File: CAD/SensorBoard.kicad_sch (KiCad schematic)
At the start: 0 parts

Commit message: Add MCU symbol
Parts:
- added MCU1: STM32U073CCT6, Package_QFP:LQFP-48_7x7mm_P0.5mm, symbol SensorBoard:STM32U073CCT6
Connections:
- new net: MCU1.23 (VSS), MCU1.35 (VSS), MCU1.47 (VSS)
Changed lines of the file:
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@@
 		(company "Cristian Cristea")
+	)
+	(symbol
+		(lib_id "SensorBoard:STM32U073CCT6")
+		(at 209.55 134.62 0)
+		(unit 1)
+		(exclude_from_sim no)
+		(in_bom yes)
+		(on_board yes)
+		(dnp no)
+		(property "Reference" "MCU1"
+			(at 195.58 92.964 0)
+			(effects
+				(font
+					(size 1.27 1.27)
+				)
+				(justify left)
+			)
+		)
+		(property "Value" " STM32U073CCT6 "
+			(at 204.47 147.32 0)
+			(effects
+				(font
+					(size 1.27 1.27)
+				)
+				(justify left)
+			)
+		)
+		(property "Footprint" "Package_QFP:LQFP-48_7x7mm_P0.5mm"
+			(at 196.85 170.18 0)
+			(effects
+				(font
+					(size 1.27 1.27)
+				)
+				(justify right)
+				(hide yes)
+			)
+		)
+		(property "Datasheet" "https://www.st.com/resource/en/datasheet/stm32u073cc.pdf"
+			(at 209.55 134.62 0)
+			(effects
+				(font
+					(size 1.27 1.27)
+				)
+				(hide yes)
+			)
+		)
+		(property "Description" "STMicroelectronics Arm Cortex-M0+ MCU, 256KB flash, 40KB RAM, 56 MHz, 1.71-3.6V, 37 GPIO, LQFP48"
+			(at 209.55 134.62 0)
+			(effects
+				(font
+					(size 1.27 1.27)
+				)
+				(hide yes)
+			)
+		)
+		(pin "33"
+		)
+		(pin "25"
+		)
+		(pin "46"
+		)
+		(pin "6"
+		)
+		(pin "14"
+		)
+		(pin "37"
+		)
+		(pin "48"
+		)
+		(pin "2"
+		)
+		(pin "42"
+		)
+		(pin "45"
+		)
+		(pin "5"
+		)
+		(pin "47"
+		)
+		(pin "21"
+		)
+		(pin "12"
+		)
+		(pin "43"
+		)
+		(pin "44"
+		)
+		(pin "10"
+		)
+		(pin "1"
+		)
+		(pin "13"
+		)
+		(pin "15"
+		)
+		(pin "11"
+		)
+		(pin "4"
+		)
+		(pin "31"
+		)
+		(pin "20"
+		)
+		(pin "16"
+		)
+		(pin "7"
+		)
+		(pin "41"
+		)
+		(pin "19"
+		)
+		(pin "39"
+		)
+		(pin "18"
+		)
+		(pin "3"
+		)
+		(pin "28"
+		)
+		(pin "17"
+		)
+		(pin "30"
+		)
+		(pin "22"
+		)
+		(pin "8"
+		)
+		(pin "34"
+		)
+		(pin "23"
+		)
+		(pin "24"
+		)
+		(pin "36"
+		)
+		(pin "9"
+		)
+		(pin "26"
+		)
+		(pin "27"
+		)
+		(pin "29"
+		)
+		(pin "40"
+		)
+		(pin "32"
+		)
+		(pin "35"
+		)
+		(pin "38"
+		)
+		(instances
+			(project ""
+				(path "/56f2708f-e6aa-4b97-8a34-e15d8ff6695d"
+					(reference "MCU1")
+					(unit 1)
+				)
+			)
+		)
 	)
 	(sheet_instances

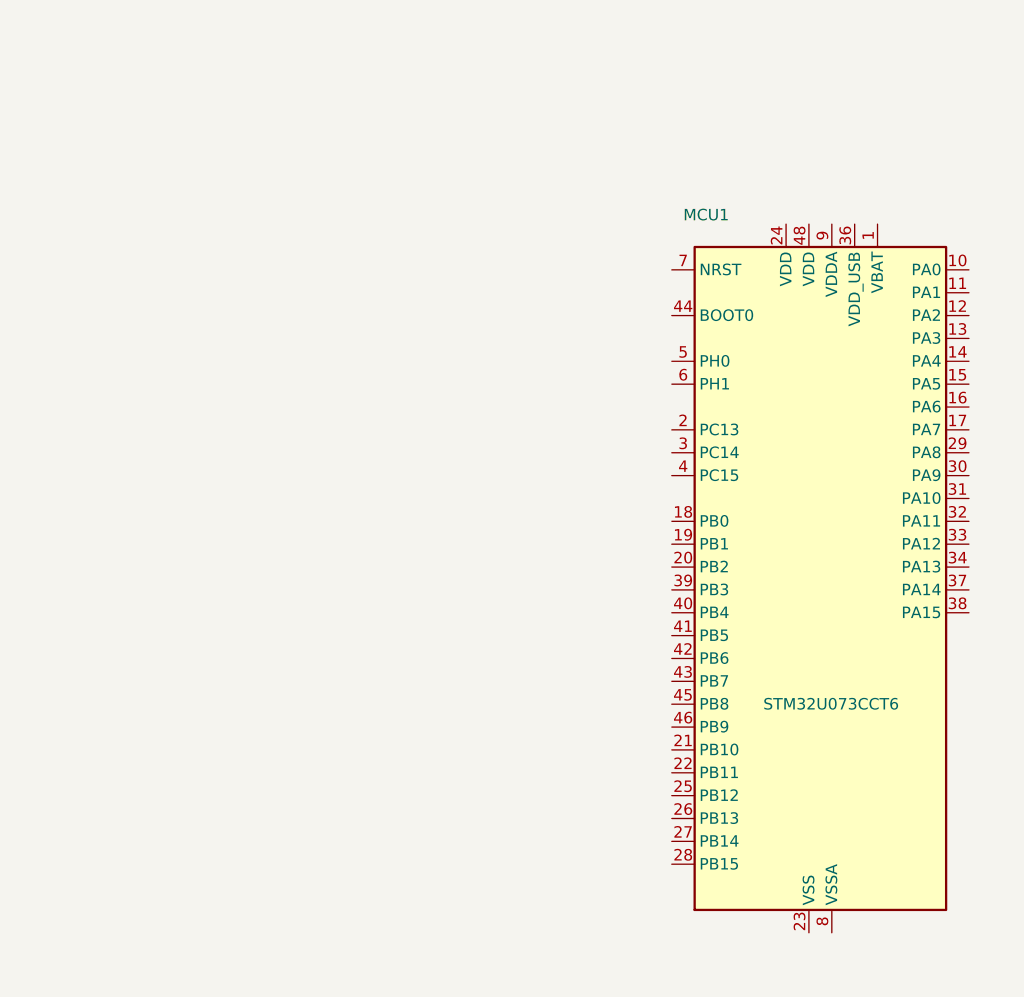
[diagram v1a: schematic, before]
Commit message: Add crystal oscillators to schematic
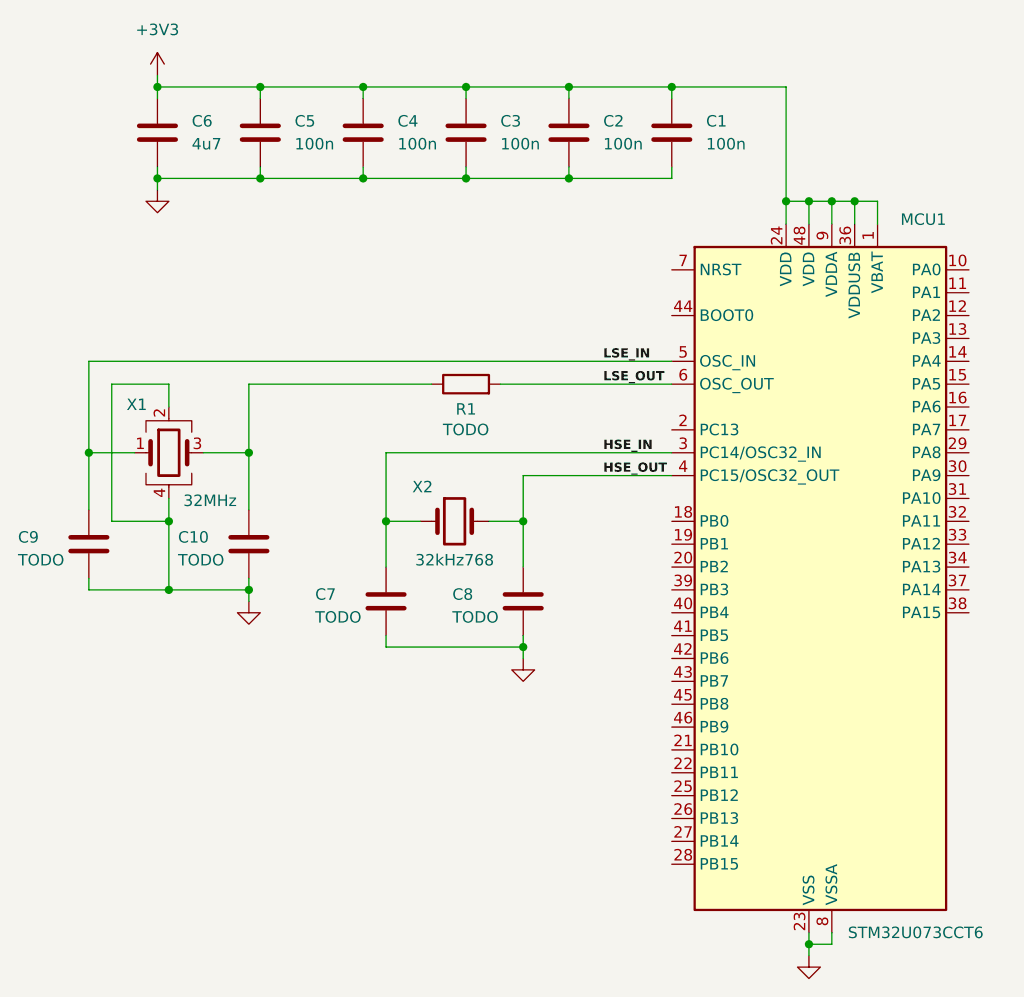
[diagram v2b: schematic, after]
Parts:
- added C1, C2, C3, C4, C5: 100n, symbol Device:C
- added C10, C7, C8, C9: TODO, symbol Device:C
- added C6: 4u7, symbol Device:C
- added R1: TODO, symbol Device:R
- added X1: 32MHz, symbol Device:Crystal_GND24
- added X2: 32kHz768, symbol Device:Crystal
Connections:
- net +3V3: now reaches MCU1.1 (VBAT)
- net +3V3: now also MCU1.24 (VDD), MCU1.36 (VDDUSB), MCU1.48 (VDD), MCU1.9 (VDDA), C1.1, C2.1, C3.1, C4.1, C5.1, C6.1
- net GND: now reaches MCU1.23 (VSS), MCU1.35 (VSS), MCU1.47 (VSS)
- net GND: now also MCU1.8 (VSSA), C1.2, C10.2, C2.2, C3.2, C4.2, C5.2, C6.2, C7.2, C8.2, C9.2, X1.2, X1.4
- net HSE_IN: now reaches MCU1.3 (PC14/OSC32_IN)
- net HSE_IN: now also C7.1, X2.1
- net HSE_OUT: now reaches MCU1.4 (PC15/OSC32_OUT)
- net HSE_OUT: now also C8.1, X2.2
- net LSE_IN: now reaches MCU1.5 (OSC_IN)
- net LSE_IN: now also C9.1, X1.1
- net LSE_OUT: now reaches MCU1.6 (OSC_OUT)
- net LSE_OUT: now also R1.2
- new net: C10.1, R1.1, X1.3

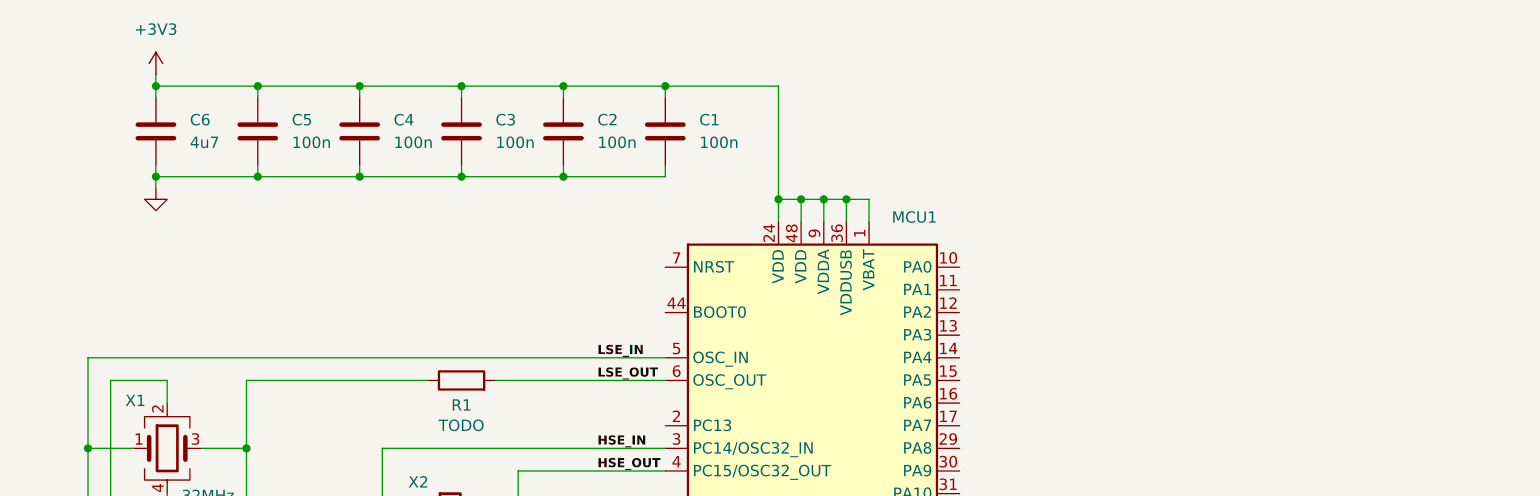
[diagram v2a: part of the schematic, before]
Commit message: Add BOOT button
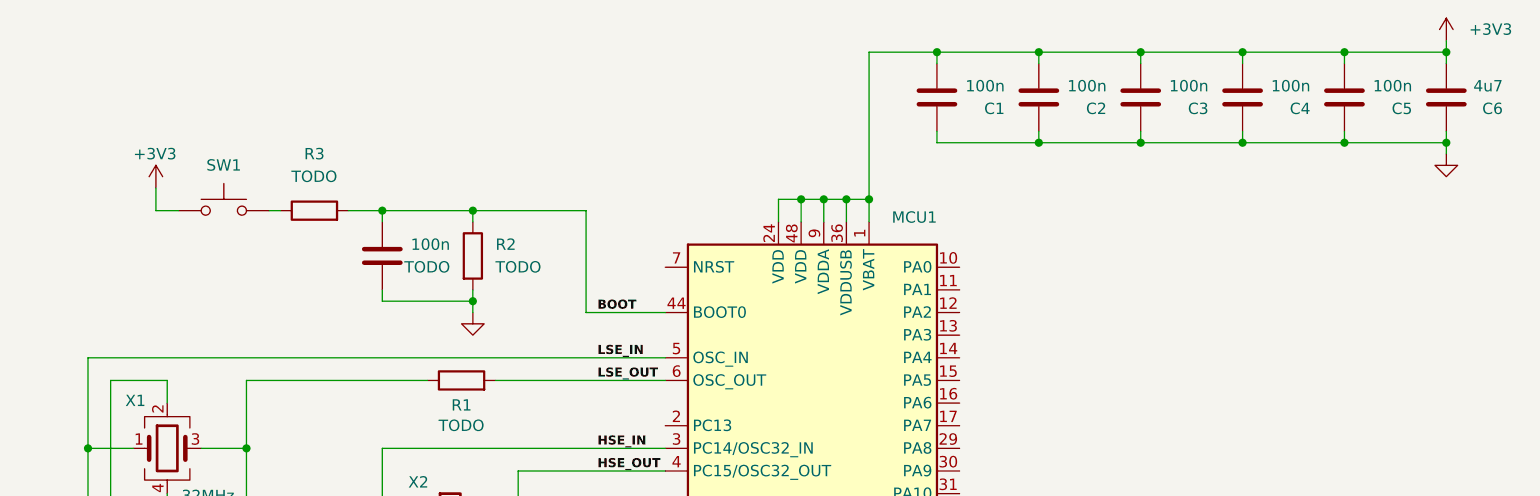
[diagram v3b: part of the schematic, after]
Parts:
- added R2, R3: TODO, symbol Device:R
- added SW1: BOOT_SW, symbol Switch:SW_Push
- added TODO: 100n, symbol Device:C
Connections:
- net +3V3: now also C1.2, C2.2, C3.2, C4.2, C5.2, C6.2, SW1.1; no longer C1.1, C2.1, C3.1, C4.1, C5.1, C6.1
- net GND: now also C1.1, C2.1, C3.1, C4.1, C5.1, C6.1, R2.2, TODO.1; no longer C1.2, C2.2, C3.2, C4.2, C5.2, C6.2
- net BOOT: now reaches MCU1.44 (BOOT0)
- net BOOT: now also R2.1, R3.2, TODO.2
- new net: R3.1, SW1.2
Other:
- moved on the sheet: C1, C2, C3, C4, C5, C6

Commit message: Further progress with power and peripherals
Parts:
- added C12, C13: 1u, symbol Device:C
- added C14: 100n, symbol Device:C
- added D1, D2: LED, symbol Device:LED
- added D3: Inolux_IN-P55TATRGB, LED_SMD:LED_Inolux_IN-P55TATRGB_PLCC6_5.0x5.5mm_P1.8mm, symbol LED:Inolux_IN-P55TATRGB
- added J1: USB C 2.0, symbol SensorBoard:USB_C_Receptacle_USB2.0
- added R10, R8, R9: 200, symbol Device:R
- added R4, R5: 5k1, symbol Device:R
- added R6, R7: 1k, symbol Device:R
- added U1: USBLC6-2SC6, Package_TO_SOT_SMD:SOT-23-6, symbol Power_Protection:USBLC6-2SC6
- added U2: MIC5365-3.3YD5, Package_TO_SOT_SMD:SOT-23-5, symbol Regulator_Linear:MIC5365-3.3YD5
- added U3: BME680, Package_LGA:Bosch_LGA-8_3x3mm_P0.8mm_ClockwisePinNumbering, symbol Sensor:BME680
- added U4: TC1047xNB, Package_TO_SOT_SMD:SOT-23, symbol Sensor_Temperature:TC1047xNB
- R2: value TODO -> 5k1
- R3: value TODO -> 200
- renumbered TODO to C11
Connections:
- net +3V3: now also C13.2, C14.2, R6.1, U2.5 (VOUT), U4.1 (V_{DD})
- net BOOT: now also MCU1.7 (NRST); no longer MCU1.44 (BOOT0)
- net GND: now also C12.1, C13.1, C14.1, D1.1 (K), D2.1 (K), D3.1 (KB), D3.2 (KR), D3.3 (KG), J1.A1 (GND), J1.A12 (GND), J1.B1 (GND), J1.B12 (GND), J1.S1 (SHIELD), R4.2, R5.2, U1.2 (GND), U2.2 (GND), U4.3 (GND)
- net HSE_IN: now also C9.1, MCU1.5 (OSC_IN), X1.1; no longer C7.1, MCU1.3 (PC14/OSC32_IN), X2.1
- net HSE_OUT: now also MCU1.6 (OSC_OUT), R1.2; no longer C8.1, MCU1.4 (PC15/OSC32_OUT), X2.2
- net LSE_IN: now also C7.1, MCU1.3 (PC14/OSC32_IN), X2.1; no longer C9.1, MCU1.5 (OSC_IN), X1.1
- net LSE_OUT: now also C8.1, MCU1.4 (PC15/OSC32_OUT), X2.2; no longer MCU1.6 (OSC_OUT), R1.2
- net ADC_TMP: now reaches MCU1.12 (PA2)
- net ADC_TMP: now also U4.2 (V_{OUT})
- net I2C_SDA: now reaches MCU1.16 (PA6)
- net I2C_SCL: now reaches MCU1.17 (PA7)
- net UART_TX: now reaches MCU1.21 (PB10)
- net UART_RX: now reaches MCU1.22 (PB11)
- net LED_R: now reaches MCU1.29 (PA8)
- net LED_R: now also R10.1
- net LED_G: now reaches MCU1.30 (PA9)
- net LED_G: now also R8.1
- net LED_B: now reaches MCU1.31 (PA10)
- net LED_B: now also R9.1
- net USB_D-: now reaches MCU1.32 (PA11)
- net USB_D-: now also U1.6 (I/O1)
- net USB_D+: now reaches MCU1.33 (PA12)
- net USB_D+: now also U1.4 (I/O2)
- net SPI_SCK: now reaches MCU1.39 (PB3)
- net SPI_MISO: now reaches MCU1.40 (PB4)
- net SPI_MOSI: now reaches MCU1.41 (PB5)
- new net: D3.5 (AR), R10.2
- new net: D3.4 (AG), R8.2
- new net: D2.2 (A), R6.2
- new net: D3.6 (AB), R9.2
- new net: D1.2 (A), R7.2
- new net +5V: C12.2, J1.A4 (VBUS), J1.A9 (VBUS), J1.B4 (VBUS), J1.B9 (VBUS), R7.1, U1.5 (VBUS), U2.1 (VIN), U2.3 (EN)
- new net USB_CC1: J1.A5 (CC1), R5.1
- new net USB_CC2: J1.B5 (CC2), R4.1
- new net USB_CD+: J1.A6 (D+), J1.B6 (D+), U1.3 (I/O2)
- new net USB_CD-: J1.A7 (D-), J1.B7 (D-), U1.1 (I/O1)
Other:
- moved on the sheet: C1, C10, C11, C2, C3, C4, C5, C6, C7, C8, C9, MCU1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

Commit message: Add BMI323 symbol and footprint
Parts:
- added U5: BMI323, SensorBoard:BMI323, symbol SensorBoard:BMI323
- R10, R3, R8, R9: value 200 -> 220
- renumbered MCU1 to MCU
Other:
- moved on the sheet: U3
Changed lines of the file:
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@@
 			)
 		)
-		(property "Value" "200"
+		(property "Value" "220"
 			(at 359.41 130.81 90)
 			(effects
@@
 			)
 		)
-		(property "Value" "200"
+		(property "Value" "220"
 			(at 364.49 124.206 90)
 			(effects
@@
 	(symbol
 		(lib_id "Sensor:BME680")
-		(at 185.42 205.74 0)
+		(at 180.34 205.74 0)
 		(unit 1)
 		(exclude_from_sim no)
@@
 		(on_board yes)
 		(dnp no)
-		(fields_autoplaced yes)
 		(property "Reference" "U3"
-			(at 173.99 204.4699 0)
+			(at 172.72 194.31 0)
 			(effects
 				(font
@@
 		)
 		(property "Value" "BME680"
-			(at 173.99 207.0099 0)
+			(at 191.77 194.31 0)
 			(effects
 				(font
@@
 		)
 		(property "Footprint" "Package_LGA:Bosch_LGA-8_3x3mm_P0.8mm_ClockwisePinNumbering"
-			(at 222.25 217.17 0)
+			(at 217.17 217.17 0)
 			(effects
 				(font
@@
 		)
 		(property "Datasheet" "https://ae-bst.resource.bosch.com/media/_tech/media/datasheets/BST-BME680-DS001.pdf"
-			(at 185.42 210.82 0)
+			(at 180.34 210.82 0)
 			(effects
 				(font
@@
 		)
 		(property "Description" "4-in-1 sensor, gas, humidity, pressure, temperature, I2C and SPI interface, 1.71-3.6V, LGA-8"
-			(at 185.42 205.74 0)
+			(at 180.34 205.74 0)
 			(effects
 				(font
@@
 			)
 		)
-		(property "Value" "200"
+		(property "Value" "220"
 			(at 346.71 53.34 90)
 			(effects
@@
 	)
 	(symbol
+		(lib_id "SensorBoard:BMI323")
+		(at 259.08 203.2 0)
+		(unit 1)
+		(exclude_from_sim no)
+		(in_bom yes)
+		(on_board yes)
+		(dnp no)
+		(property "Reference" "U5"
+			(at 247.65 194.31 0)
+			(effects
+				(font
+					(size 1.27 1.27)
+				)
+				(justify left)
+			)
+		)
+		(property "Value" "BMI323"
+			(at 268.224 194.31 0)
+			(do_not_autoplace yes)
+			(effects
+				(font
+					(size 1.27 1.27)
+				)
+			)
+		)
+		(property "Footprint" "SensorBoard:BMI323"
+			(at 252.73 196.85 0)
+			(effects
+				(font
+					(size 1.27 1.27)
+				)
+				(hide yes)
+			)
+		)
+		(property "Datasheet" "https://www.bosch-sensortec.com/media/boschsensortec/downloads/datasheets/bst-bmi323-ds000.pdf"
+			(at 252.73 196.85 0)
+			(effects
+				(font
+					(size 1.27 1.27)
+				)
+				(hide yes)
+			)
+		)
+		(property "Description" ""
+			(at 252.73 196.85 0)
+			(effects
+				(font
+					(size 1.27 1.27)
+				)
+				(hide yes)
+			)
+		)
+		(pin "13"
+		)
+		(pin "7"
+		)
+		(pin "9"
+		)
+		(pin "4"
+		)
+		(pin "5"
+		)
+		(pin "8"
+		)
+		(pin "6"
+		)
+		(pin "14"
+		)
+		(pin "12"
+		)
+		(pin "1"
+		)
+		(instances
+			(project ""
+				(path "/56f2708f-e6aa-4b97-8a34-e15d8ff6695d"
+					(reference "U5")
+					(unit 1)
+				)
+			)
+		)
+	)
+	(symbol
 		(lib_id "power:+3V3")
 		(at 205.74 54.61 0)
@@
 		(on_board yes)
 		(dnp no)
-		(property "Reference" "MCU1"
+		(property "Reference" "MCU"
 			(at 82.55 148.082 0)
 			(effects
@@
 			(project ""
 				(path "/56f2708f-e6aa-4b97-8a34-e15d8ff6695d"
-					(reference "MCU1")
+					(reference "MCU")
 					(unit 1)
 				)
@@
 			)
 		)
-		(property "Value" "200"
+		(property "Value" "220"
 			(at 364.49 137.16 90)
 			(effects
